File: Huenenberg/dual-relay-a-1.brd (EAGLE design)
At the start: 78.4 x 49.5 mm, 40 parts, among them J10 LARGE-SOLDERPAD, J11 LARGE-SOLDERPAD, J12 LARGE-SOLDERPAD, J13 LARGE-SOLDERPAD, J14 LARGE-SOLDERPAD, J15 LARGE-SOLDERPAD, J16 LARGE-SOLDERPAD, J17 LARGE-SOLDERPAD, J18 LARGE-SOLDERPAD, J19 LARGE-SOLDERPAD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

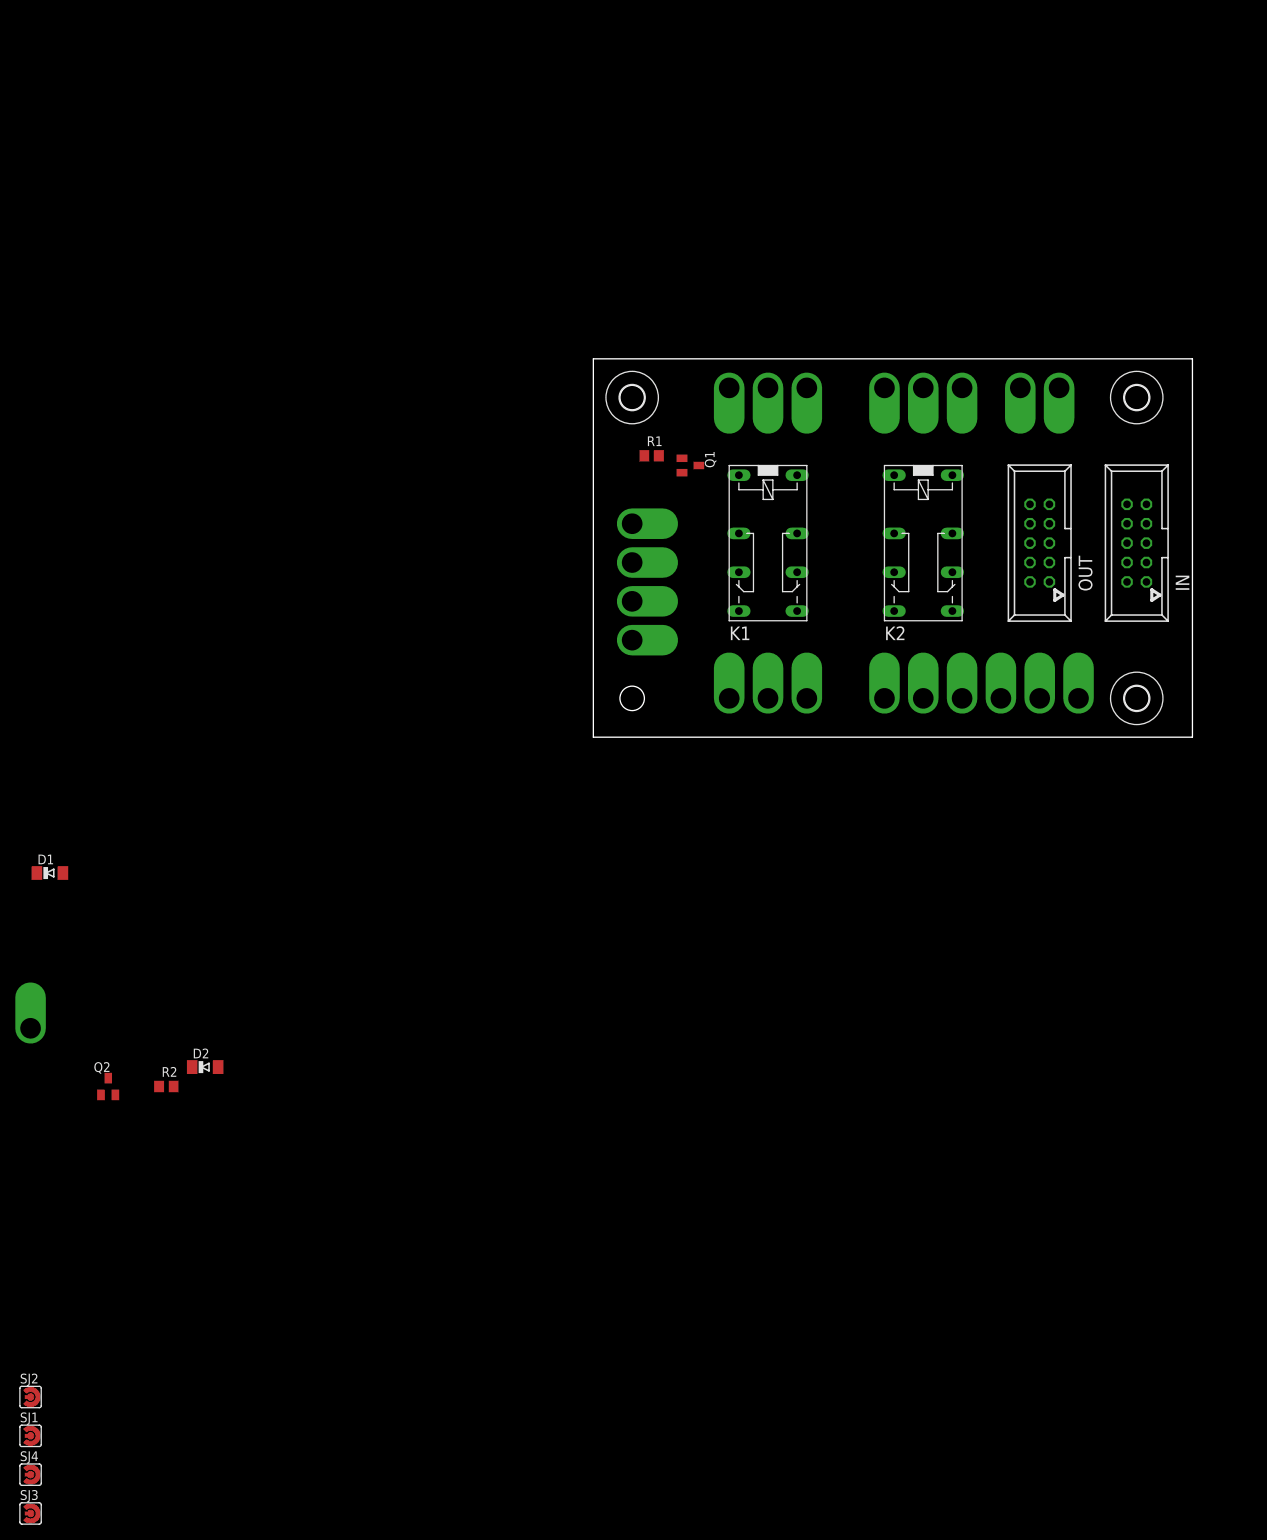
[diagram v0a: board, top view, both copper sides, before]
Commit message: Adds values to the large solderpads that explain what should be connected.
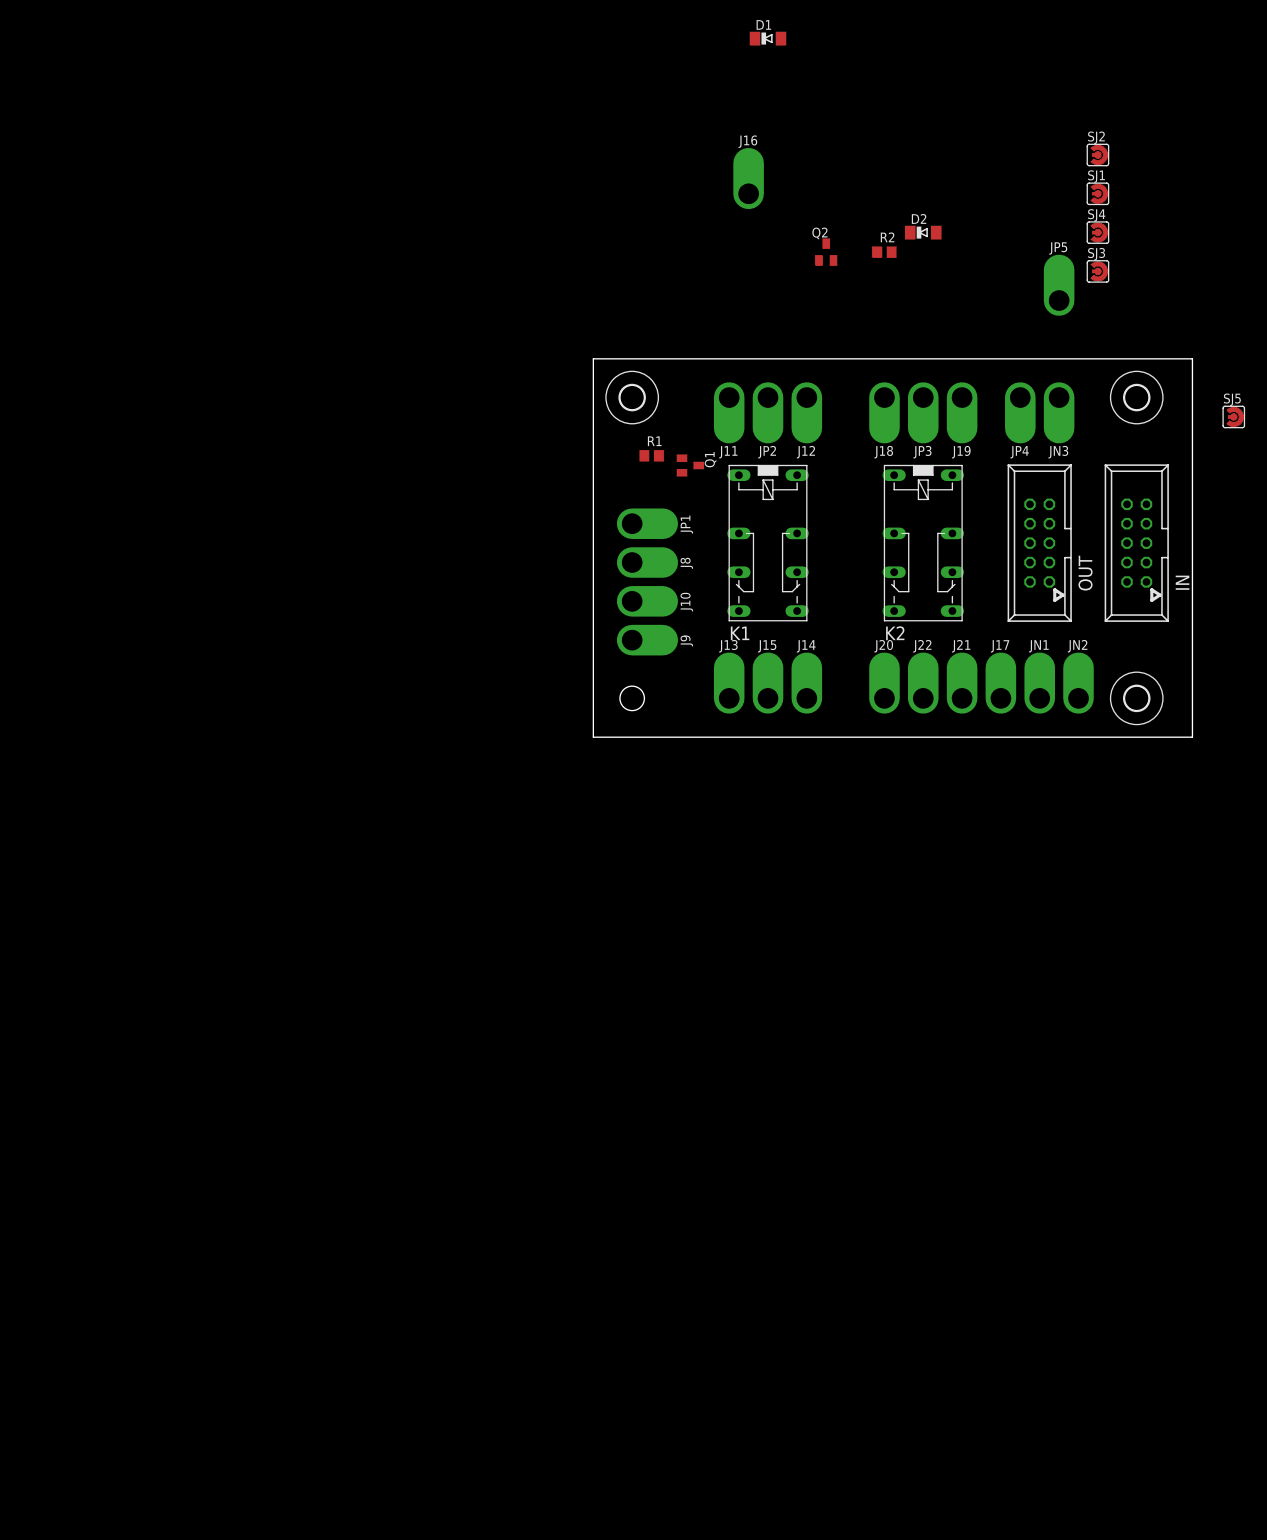
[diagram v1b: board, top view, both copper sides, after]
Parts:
- added JP5: XTRA, eagleparts:LARGE-SOLDERPAD
- added SJ5: 12VIN, trainlib:SJ_RND2
- IN: value PORTA -> IN
- J10, J17: value LARGE-SOLDERPAD -> HI
- J11, J13, J18, J20: value LARGE-SOLDERPAD -> REV
- J12, J14, J19, J21: value LARGE-SOLDERPAD -> NORM
- J15, J22: value LARGE-SOLDERPAD -> COM
- J16, J9: value LARGE-SOLDERPAD -> LOW
- J8, JN1, JN2, JN3: value LARGE-SOLDERPAD -> GND
- JP1, JP2, JP3, JP4: value LARGE-SOLDERPAD -> 12V
- OUT: value PORTA -> OUT
- SJ1: value (none) -> CH1_ACTLOW
- SJ2: value (none) -> CH1_ARD
- SJ3: value (none) -> CH2_ACTLOW
- SJ4: value (none) -> CH2_ARD
- moved SJ1 214.3 mm to (66.0, 71.1)
- moved SJ2 214.3 mm to (66.0, 76.2)
- moved SJ3 214.3 mm to (66.0, 61.0)
- moved SJ4 214.3 mm to (66.0, 66.0)
- moved D1 144.1 mm to (22.9, 91.4)
- moved D2 144.1 mm to (43.2, 66.0)
- moved J16 144.1 mm to (20.3, 71.1)
- moved Q2 144.1 mm to (30.5, 63.5)
- moved R2 144.1 mm to (38.1, 63.5)
- moved J11 1.27 mm to (17.8, 44.5)
- moved J12 1.27 mm to (27.9, 44.5)
- moved J18 1.27 mm to (38.1, 44.5)
- moved J19 1.27 mm to (48.3, 44.5)
- moved JN3 1.27 mm to (61.0, 44.5)
- moved JP2 1.27 mm to (22.9, 44.5)
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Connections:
- net +12V: now also OUT.6, SJ5.P$2
- net +5V: now also SJ5.P$1; no longer OUT.6
- net N$22: now also JP5.P$1
